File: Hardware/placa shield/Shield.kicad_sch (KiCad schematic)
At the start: 20 parts, among them J1 HC-05 connector, J6 Dimmer module, Q1 2N7000, SW5 SW_DIP_x04, X3 ST-MORPHO-CN7, X4 ST-MORPHO-CN10

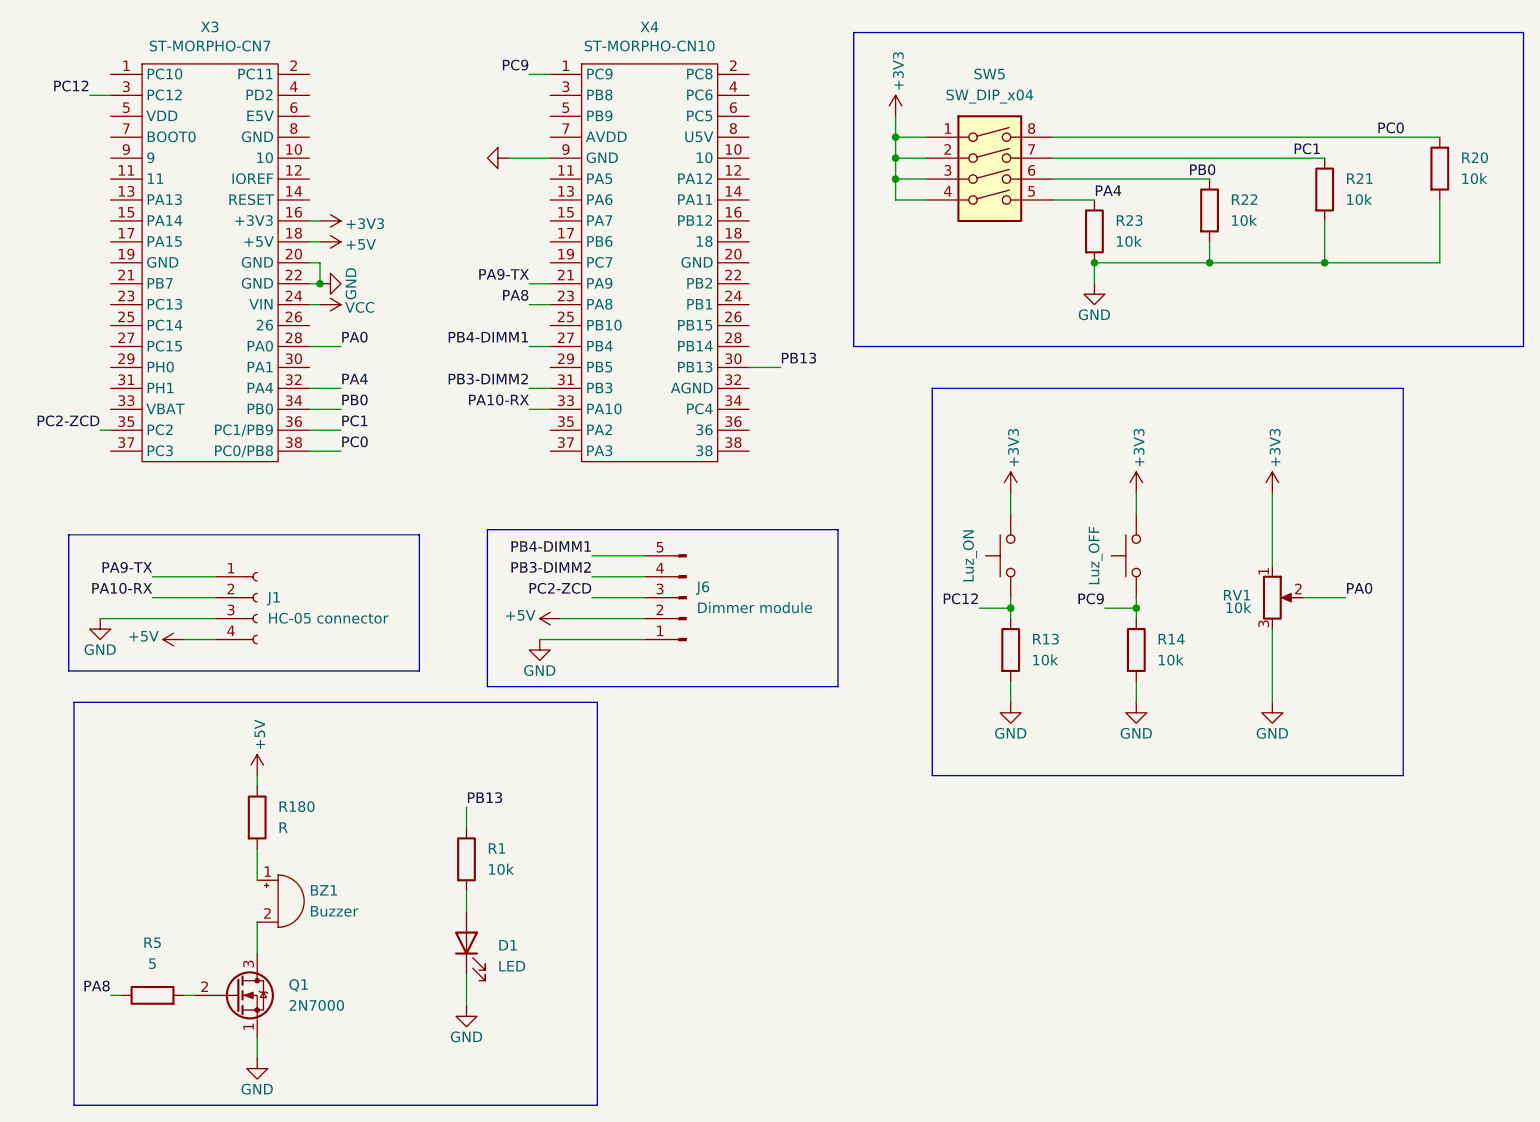
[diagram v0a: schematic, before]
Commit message: ajustes hardware
renombrar carpeta kicad -> hardware y anotaciones planos
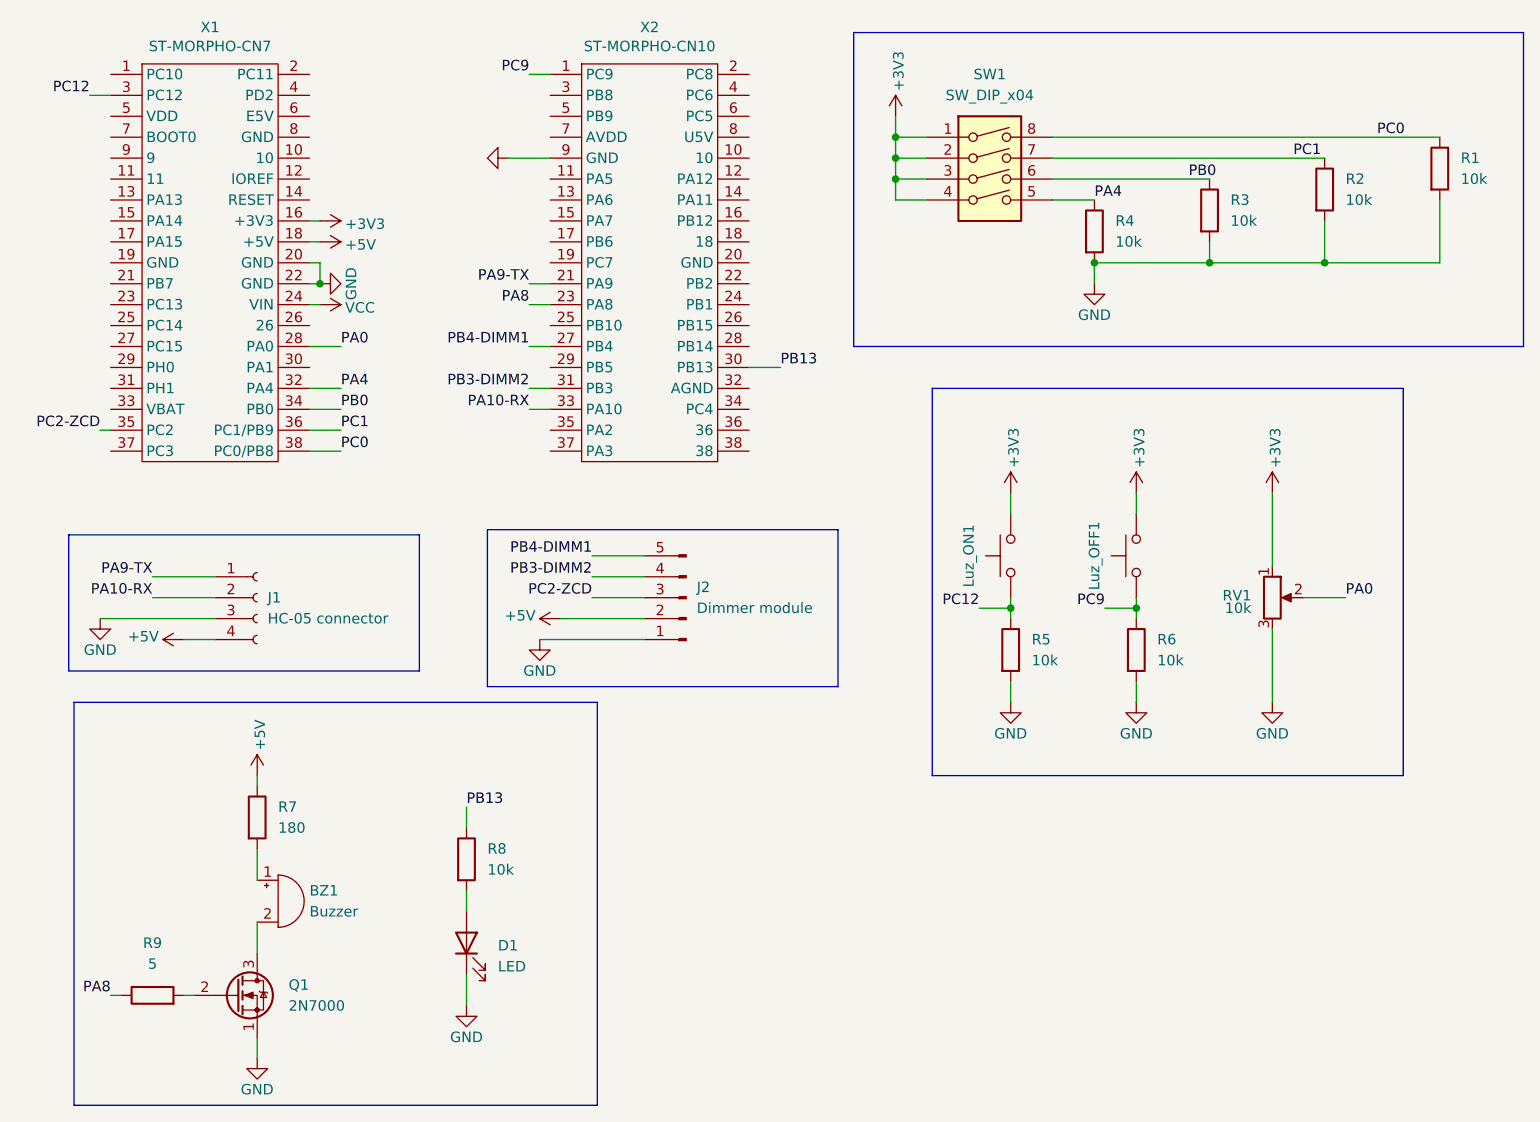
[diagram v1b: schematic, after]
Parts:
- R7: renamed from R180; value R -> 180
- renumbered J6 to J2, Luz_OFF to Luz_OFF1, Luz_ON to Luz_ON1, R20 to R1, R21 to R2, R22 to R3, R23 to R4, R13 to R5, R14 to R6, R1 to R8, R5 to R9, SW5 to SW1, X3 to X1, X4 to X2
